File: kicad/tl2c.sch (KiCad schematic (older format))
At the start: 35 parts, among them IC101 ATTINY20-X, P101 12VDC, P102 I2C Master, P103 Spare, P104 TPI Header, P105 LED_DRIVER, P106 240VAC, P107 LED_DRIVER, P108 LED_OUT, P109 5VDC, SW101 TL3315NF160Q

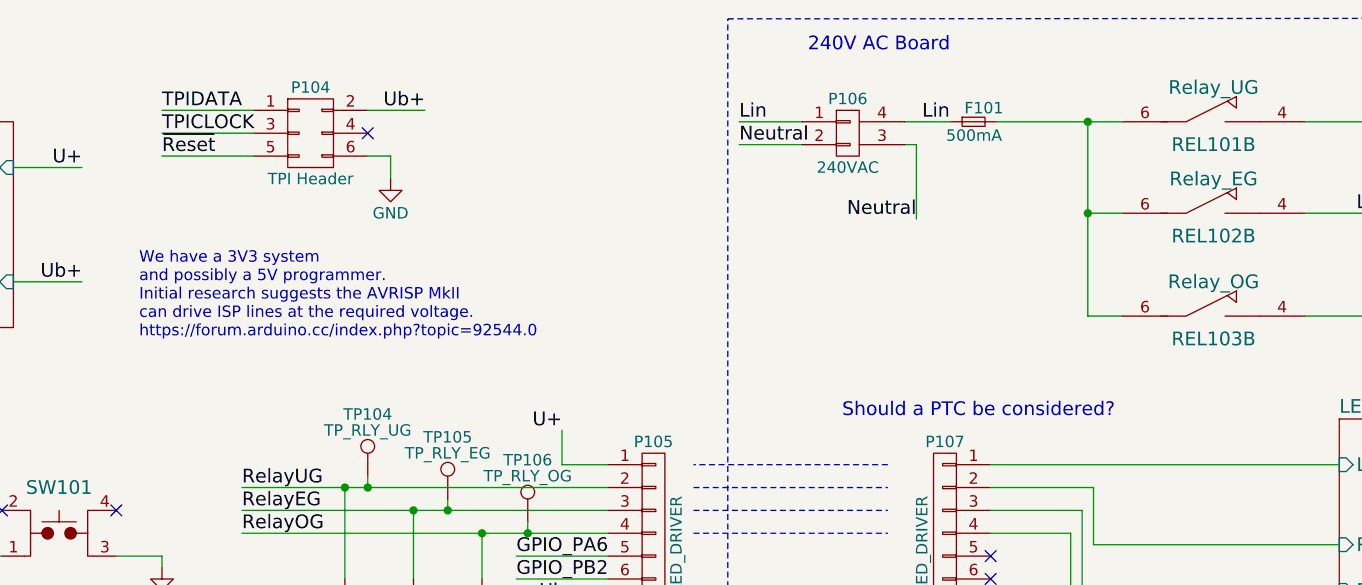
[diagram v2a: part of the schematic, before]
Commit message: Made a correction to a net label
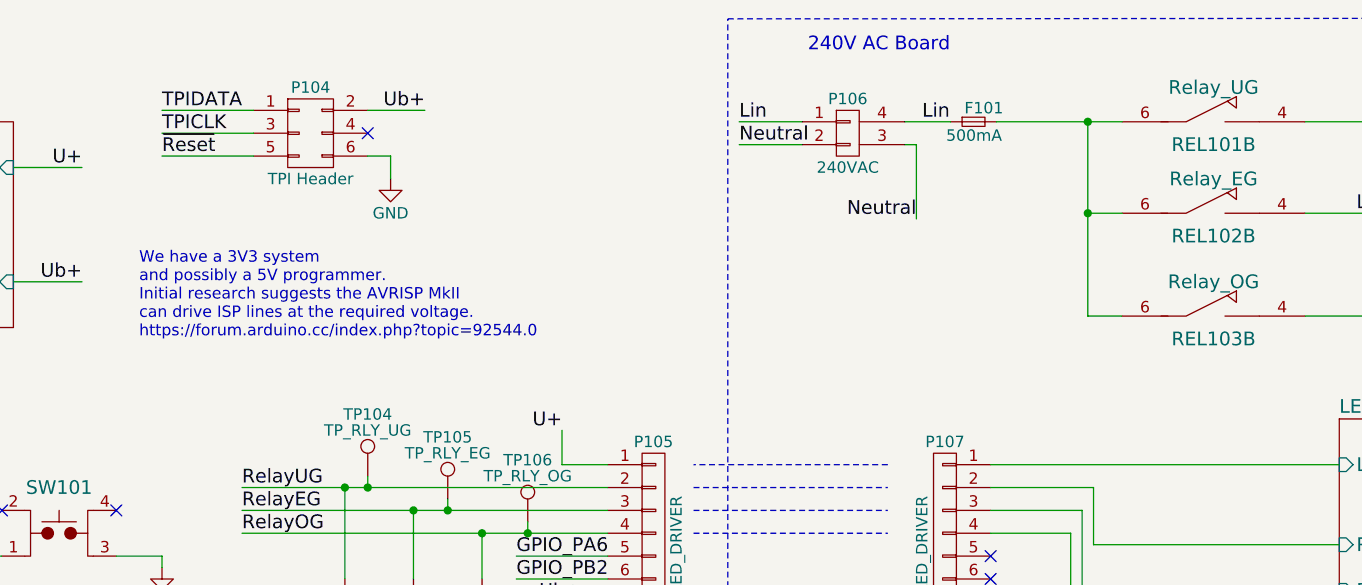
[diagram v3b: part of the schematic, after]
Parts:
- P104: footprint Pin_Headers:Pin_Header_Straight_2x03 -> tl2c-footprint:TC2030-IDC-FP_ISP_Connector
- P109: footprint Pin_Headers:Pin_Header_Straight_1x02 -> Pin_Headers:Pin_Header_Straight_1x02_Pitch2.54mm
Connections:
- net TPICLOCK is gone; now on net TPICLK: P104.3 (P3)
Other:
- note removed: "Should a PTC be considered?"
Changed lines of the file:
@@
 Ub+
 $Comp
-L GND #PWR107
+L GND #PWR01
 U 1 1 584C3309
 P 3700 6200
-F 0 "#PWR107" H 3700 5950 50  0001 C CNN
+F 0 "#PWR01" H 3700 5950 50  0001 C CNN
 F 1 "GND" H 3700 6050 50  0000 C CNN
 F 2 "" H 3700 6200 50  0000 C CNN
@@
 Text Label 3850 1100 0    60   ~ 0
 TPIDATA
-Text Label 3850 1200 0    60   ~ 0
-TPICLOCK
 Text Label 5000 1100 2    60   ~ 0
 Ub+
 $Comp
-L GND #PWR110
+L GND #PWR02
 U 1 1 584C39BE
 P 4850 1400
-F 0 "#PWR110" H 4850 1150 50  0001 C CNN
+F 0 "#PWR02" H 4850 1150 50  0001 C CNN
 F 1 "GND" H 4850 1250 50  0000 C CNN
 F 2 "" H 4850 1400 50  0000 C CNN
@@
 $EndComp
 $Comp
-L GND #PWR105
+L GND #PWR03
 U 1 1 584C4458
 P 2850 5100
-F 0 "#PWR105" H 2850 4850 50  0001 C CNN
+F 0 "#PWR03" H 2850 4850 50  0001 C CNN
 F 1 "GND" H 2850 4950 50  0000 C CNN
 F 2 "" H 2850 5100 50  0000 C CNN
@@
 $EndComp
 $Comp
-L GND #PWR114
+L GND #PWR04
 U 1 1 584C7124
 P 7450 5900
-F 0 "#PWR114" H 7450 5650 50  0001 C CNN
+F 0 "#PWR04" H 7450 5650 50  0001 C CNN
 F 1 "GND" H 7450 5750 50  0000 C CNN
 F 2 "" H 7450 5900 50  0000 C CNN
@@
 SCL
 $Comp
-L GND #PWR104
+L GND #PWR05
 U 1 1 584C7C99
 P 1400 3250
-F 0 "#PWR104" H 1400 3000 50  0001 C CNN
+F 0 "#PWR05" H 1400 3000 50  0001 C CNN
 F 1 "GND" H 1400 3100 50  0000 C CNN
 F 2 "" H 1400 3250 50  0000 C CNN
@@
 Neutral
 $Comp
-L GND #PWR108
+L GND #PWR06
 U 1 1 584CB28B
 P 3850 3100
-F 0 "#PWR108" H 3850 2850 50  0001 C CNN
+F 0 "#PWR06" H 3850 2850 50  0001 C CNN
 F 1 "GND" H 3850 2950 50  0000 C CNN
 F 2 "" H 3850 3100 50  0000 C CNN
@@
 Ub+
 $Comp
-L GND #PWR102
+L GND #PWR07
 U 1 1 584DF6BA
 P 1200 1600
-F 0 "#PWR102" H 1200 1350 50  0001 C CNN
+F 0 "#PWR07" H 1200 1350 50  0001 C CNN
 F 1 "GND" H 1200 1450 50  0000 C CNN
 F 2 "" H 1200 1600 50  0000 C CNN
@@
 $EndComp
 $Comp
-L GND #PWR101
+L GND #PWR08
 U 1 1 584E33BE
 P 1100 4700
-F 0 "#PWR101" H 1100 4450 50  0001 C CNN
+F 0 "#PWR08" H 1100 4450 50  0001 C CNN
 F 1 "GND" H 1100 4550 50  0000 C CNN
 F 2 "" H 1100 4700 50  0000 C CNN
@@
 $EndSheet
 $Comp
-L GND #PWR113
+L GND #PWR09
 U 1 1 58541B90
 P 5700 3425
-F 0 "#PWR113" H 5700 3175 50  0001 C CNN
+F 0 "#PWR09" H 5700 3175 50  0001 C CNN
 F 1 "GND" H 5700 3275 50  0000 C CNN
 F 2 "" H 5700 3425 50  0000 C CNN
@@
 $EndComp
 $Comp
-L GND #PWR109
+L GND #PWR010
 U 1 1 5856AF1B
 P 4650 4050
-F 0 "#PWR109" H 4650 3800 50  0001 C CNN
+F 0 "#PWR010" H 4650 3800 50  0001 C CNN
 F 1 "GND" H 4650 3900 50  0000 C CNN
 F 2 "" H 4650 4050 50  0000 C CNN
@@
 $EndComp
 $Comp
-L GND #PWR111
+L GND #PWR011
 U 1 1 5856B284
 P 4950 4050
-F 0 "#PWR111" H 4950 3800 50  0001 C CNN
+F 0 "#PWR011" H 4950 3800 50  0001 C CNN
 F 1 "GND" H 4950 3900 50  0000 C CNN
 F 2 "" H 4950 4050 50  0000 C CNN
@@
 $EndComp
 $Comp
-L GND #PWR112
+L GND #PWR012
 U 1 1 5856B510
 P 5250 4050
-F 0 "#PWR112" H 5250 3800 50  0001 C CNN
+F 0 "#PWR012" H 5250 3800 50  0001 C CNN
 F 1 "GND" H 5250 3900 50  0000 C CNN
 F 2 "" H 5250 4050 50  0000 C CNN
@@
 $EndComp
 $Comp
-L GNDA #PWR115
+L GNDA #PWR013
 U 1 1 5856E00B
 P 7575 3600
-F 0 "#PWR115" H 7575 3350 50  0001 C CNN
+F 0 "#PWR013" H 7575 3350 50  0001 C CNN
 F 1 "GNDA" H 7575 3450 50  0000 C CNN
 F 2 "" H 7575 3600 50  0000 C CNN
@@
 Text Notes 7225 4100 0    60   ~ 0
 TODO - Change the relay to  AZ7705T-1A-12DEF - Conrad.\nor FIN 43.41.7 12V - Reichelt
-Text Notes 6825 2450 0    60   ~ 0
-Should a PTC be considered?
 Text Label 5600 2500 2    60   ~ 0
 U+
@@
 F 0 "P104" H 4500 1400 50  0000 C CNN
 F 1 "TPI Header" H 4500 1000 50  0000 C CNN
-F 2 "Pin_Headers:Pin_Header_Straight_2x03" H 4500 0   50  0001 C CNN
+F 2 "tl2c-footprint:TC2030-IDC-FP_ISP_Connector" H 4500 0   50  0001 C CNN
 F 3 "" H 4500 0   50  0000 C CNN
 F 4 "Value" H 4500 1200 60  0001 C CNN "MFP"
@@
 $EndComp
 $Comp
-L GND #PWR106
+L GND #PWR014
 U 1 1 5867873E
 P 3050 3600
-F 0 "#PWR106" H 3050 3350 50  0001 C CNN
+F 0 "#PWR014" H 3050 3350 50  0001 C CNN
 F 1 "GND" H 3050 3450 50  0000 C CNN
 F 2 "" H 3050 3600 50  0000 C CNN
@@
 F 0 "P109" H 900 2050 50  0000 C CNN
 F 1 "5VDC" V 1000 1900 50  0000 C CNN
-F 2 "Pin_Headers:Pin_Header_Straight_1x02" H 900 1900 50  0001 C CNN
+F 2 "Pin_Headers:Pin_Header_Straight_1x02_Pitch2.54mm" H 900 1900 50  0001 C CNN
 F 3 "" H 900 1900 50  0000 C CNN
 F 4 "Value" H 900 1900 60  0001 C CNN "MFP"
@@
 	1100 1850 1400 1850
 $Comp
-L GND #PWR103
+L GND #PWR015
 U 1 1 589A5184
 P 1250 2100
-F 0 "#PWR103" H 1250 1850 50  0001 C CNN
+F 0 "#PWR015" H 1250 1850 50  0001 C CNN
 F 1 "GND" H 1250 1950 50  0000 C CNN
 F 2 "" H 1250 2100 50  0000 C CNN
@@
 Text Notes 550  2200 0    60   ~ 0
 Ub+ for \nprogramming
+Text Label 3850 1200 0    60   ~ 0
+TPICLK
 $EndSCHEMATC
